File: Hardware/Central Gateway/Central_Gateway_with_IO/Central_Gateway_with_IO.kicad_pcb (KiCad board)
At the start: 2 copper layers, 1 part

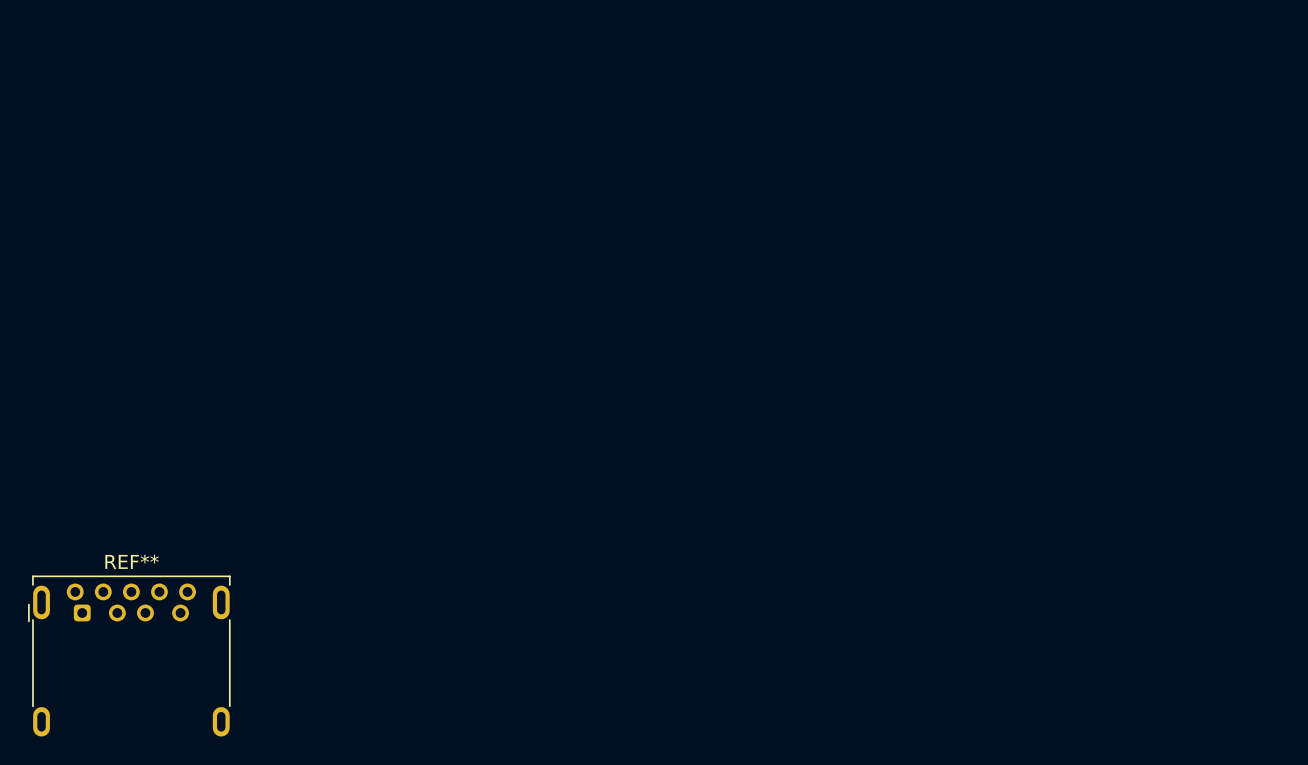
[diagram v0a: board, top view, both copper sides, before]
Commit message: Began KiCAD schematic
Added following items to schematic:
STM32h747
2x MCP 2551
2x MCP 2515
2x Crystal Oscillator
4x Capacitors
2x screw terminals

Uhh I hope I did this right
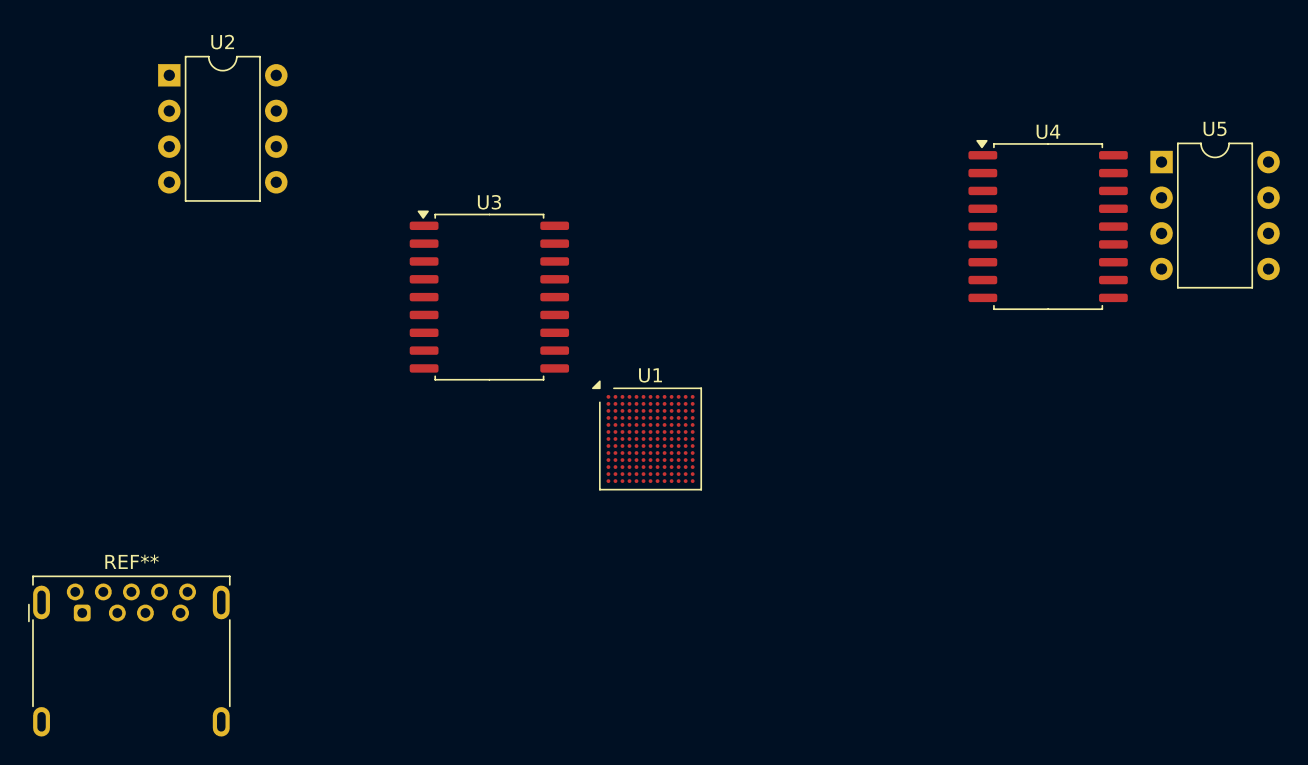
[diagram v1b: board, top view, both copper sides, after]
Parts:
- added U1: STM32H747AIIx, Package_BGA:UFBGA-169_7x7mm_Layout13x13_P0.5mm, F.Cu at (191.0, 83.1)
- added U2: MCP2551-I-P, Package_DIP:DIP-8_W7.62mm, F.Cu at (156.7, 57.2)
- added U3: MCP2515-xSO, Package_SO:SOIC-18W_7.5x11.6mm_P1.27mm, F.Cu at (179.5, 73.0)
- added U4: MCP2515-xSO, Package_SO:SOIC-18W_7.5x11.6mm_P1.27mm, F.Cu at (219.3, 68.0)
- added U5: MCP2551-I-P, Package_DIP:DIP-8_W7.62mm, F.Cu at (227.4, 63.4)
